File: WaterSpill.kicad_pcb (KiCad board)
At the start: 2 copper layers, 31.8 x 36.8 mm, 29 parts, among them J1 FTDI, J2 Water_Smoke, J3 A2D, J4 DeepSleep, J5 Water_JMPR, Q1 2N3904, SW1 PGM, SW2 RESET, U1 ESP-12E, U2 74HCT132

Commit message: Silk Screen text added
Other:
- board text added: "+"
- board text added: "A2D"
- board text added: "Deep"
- board text added: "ESP8266 WaterSpill/SmokeDector Sensor (c) 2019/01/23 - Guy Turcotte"
- board text added: "Pg"
- board text added: "RST"
- board text added: "g"
- board text added: "in"
- board text added: "r"
- board text added: "t"
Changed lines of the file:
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@@
   (general
     (thickness 1.6)
-    (drawings 8)
+    (drawings 18)
     (tracks 217)
     (zones 0)
@@
   (page A4)
   (layers
-    (0 F.Cu signal hide)
-    (31 B.Cu signal)
+    (0 F.Cu signal)
+    (31 B.Cu signal hide)
     (32 B.Adhes user hide)
     (33 F.Adhes user hide)
-    (34 B.Paste user)
-    (35 F.Paste user hide)
-    (36 B.SilkS user)
-    (37 F.SilkS user hide)
-    (38 B.Mask user)
-    (39 F.Mask user hide)
+    (34 B.Paste user hide)
+    (35 F.Paste user)
+    (36 B.SilkS user hide)
+    (37 F.SilkS user)
+    (38 B.Mask user hide)
+    (39 F.Mask user)
     (40 Dwgs.User user hide)
     (41 Cmts.User user hide)
@@
     (44 Edge.Cuts user)
     (45 Margin user hide)
-    (46 B.CrtYd user)
-    (47 F.CrtYd user hide)
-    (48 B.Fab user)
-    (49 F.Fab user hide)
+    (46 B.CrtYd user hide)
+    (47 F.CrtYd user)
+    (48 B.Fab user hide)
+    (49 F.Fab user)
   )
   (setup
@@
     )
   )
+  (gr_text Pg (at 58.239 50.8) (layer F.SilkS)
+    (effects (font (size 1.3 1.3) (thickness 0.3)))
+  )
+  (gr_text RST (at 30.099 50.8) (layer F.SilkS)
+    (effects (font (size 1.3 1.3) (thickness 0.3)))
+  )
+  (gr_text t (at 55.118 30.226) (layer F.SilkS)
+    (effects (font (size 1.5 1.5) (thickness 0.3)))
+  )
+  (gr_text r (at 54.991 27.686) (layer F.SilkS)
+    (effects (font (size 1.5 1.5) (thickness 0.3)))
+  )
+  (gr_text g (at 54.991 25.019) (layer F.SilkS)
+    (effects (font (size 1.5 1.5) (thickness 0.3)))
+  )
+  (gr_text in (at 57.15 48.133) (layer F.SilkS)
+    (effects (font (size 1.5 1.5) (thickness 0.3)))
+  )
+  (gr_text Deep (at 33.201 36.068 90) (layer F.SilkS)
+    (effects (font (size 1.5 1.5) (thickness 0.3)))
+  )
+  (gr_text + (at 32.385 43.053) (layer F.SilkS)
+    (effects (font (size 1.5 1.5) (thickness 0.3)))
+  )
+  (gr_text A2D (at 33.274 22.733 90) (layer F.SilkS)
+    (effects (font (size 1.5 1.5) (thickness 0.3)))
+  )
+  (gr_text "ESP8266 WaterSpill/SmokeDector Sensor\n(c) 2019/01/23 -  Guy Turcotte" (at 43.226 51.2) (layer B.SilkS)
+    (effects (font (size 1.1 0.9) (thickness 0.2)) (justify mirror))
+  )
   (gr_arc (start 58.42 52.07) (end 58.42 53.34) (angle -90) (layer Edge.Cuts) (width 0.15))

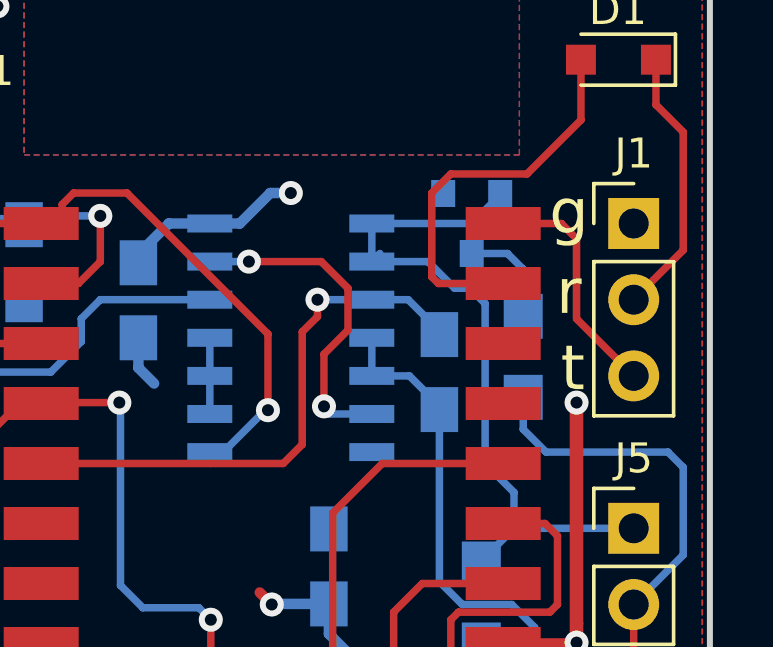
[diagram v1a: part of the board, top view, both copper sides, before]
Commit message: Corrected transistor footprint
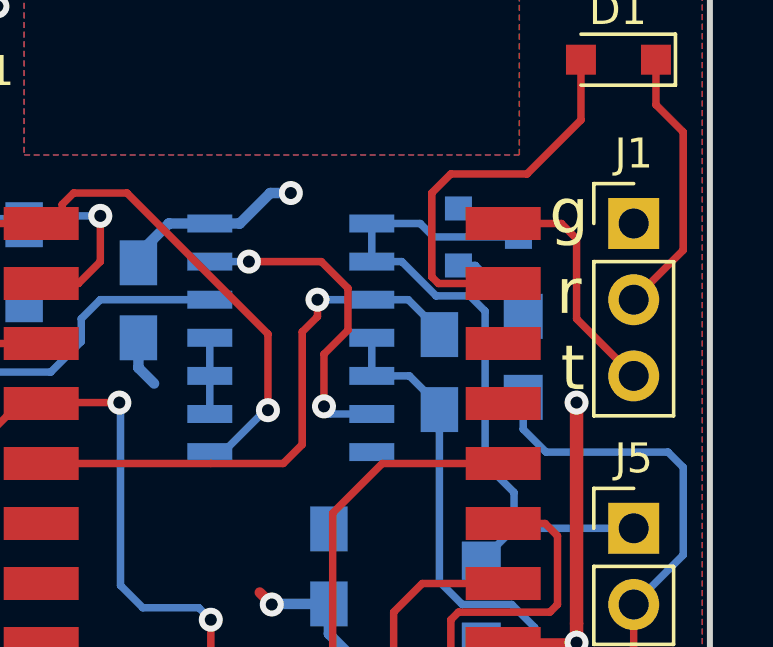
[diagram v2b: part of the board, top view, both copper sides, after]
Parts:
- J1: value FTDI -> Conn_01x03_Male
- J2: value Water_Smoke -> Conn_01x02_Male
- J3: value A2D -> Conn_01x03_Male
- J4: value DeepSleep -> Conn_01x03_Male
- J5: value Water_JMPR -> Conn_01x02_Male
- Q1: value 2N3904 -> MMBT3904; footprint TO_SOT_Packages_SMD:SOT-23 -> Package_TO_SOT_SMD:SOT-23
- SW1: value PGM -> SW_Push
- SW2: value RESET -> SW_Push
- U2: value 74HCT132 -> 74HC132
- moved Q1 0.71 mm to (52.3, 25.8), turned to 0 degrees
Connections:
- Q1 pad 1: GND -> Net-(Q1-Pad1)
- Q1 pad 2: Net-(J5-Pad1) -> GND
- Q1 pad 3: Net-(Q1-Pad3) -> Net-(J5-Pad1)
- R8 pad 2: Net-(Q1-Pad3) -> Net-(Q1-Pad1)
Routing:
- net Net-(Q1-Pad3): track 3.51 -> 0.00 mm
- net Net-(Q1-Pad1): track 0.00 -> 2.92 mm

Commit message: Added Gerber files for etching
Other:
- board text added: "G"
- board text added: "IN"
- board text added: "PG"
- board text added: "R"
- board text added: "T"
- board text removed: "Pg"
- board text removed: "g"
- board text removed: "in"
- board text removed: "r"
- board text removed: "t"
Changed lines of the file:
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@@
   (page A4)
   (layers
-    (0 F.Cu signal hide)
-    (31 B.Cu signal)
+    (0 F.Cu signal)
+    (31 B.Cu signal hide)
     (32 B.Adhes user hide)
     (33 F.Adhes user hide)
-    (34 B.Paste user)
-    (35 F.Paste user hide)
-    (36 B.SilkS user)
-    (37 F.SilkS user hide)
-    (38 B.Mask user)
-    (39 F.Mask user hide)
+    (34 B.Paste user hide)
+    (35 F.Paste user)
+    (36 B.SilkS user hide)
+    (37 F.SilkS user)
+    (38 B.Mask user hide)
+    (39 F.Mask user)
     (40 Dwgs.User user hide)
     (41 Cmts.User user hide)
@@
     (44 Edge.Cuts user)
     (45 Margin user hide)
-    (46 B.CrtYd user)
+    (46 B.CrtYd user hide)
     (47 F.CrtYd user hide)
-    (48 B.Fab user)
+    (48 B.Fab user hide)
     (49 F.Fab user hide)
   )
@@
       (outputformat 1)
       (mirror false)
-      (drillshape 1)
+      (drillshape 0)
       (scaleselection 1)
-      (outputdirectory ""))
+      (outputdirectory "gerbers/"))
   )
   (net 0 "")
@@
     )
   )
-  (gr_text Pg (at 58.239 50.8) (layer F.SilkS)
+  (gr_text PG (at 58.239 50.8) (layer F.SilkS)
     (effects (font (size 1.3 1.3) (thickness 0.3)))
   )
@@
     (effects (font (size 1.3 1.3) (thickness 0.3)))
   )
-  (gr_text t (at 55.118 30.226) (layer F.SilkS)
+  (gr_text T (at 55.118 30.607) (layer F.SilkS)
     (effects (font (size 1.5 1.5) (thickness 0.3)))
   )
-  (gr_text r (at 54.991 27.686) (layer F.SilkS)
+  (gr_text R (at 54.991 27.94) (layer F.SilkS)
     (effects (font (size 1.5 1.5) (thickness 0.3)))
   )
-  (gr_text g (at 54.991 25.019) (layer F.SilkS)
+  (gr_text G (at 54.991 25.019) (layer F.SilkS)
     (effects (font (size 1.5 1.5) (thickness 0.3)))
   )
-  (gr_text in (at 57.15 48.133) (layer F.SilkS)
+  (gr_text IN (at 58.039 48.514) (layer F.SilkS)
     (effects (font (size 1.5 1.5) (thickness 0.3)))
   )
